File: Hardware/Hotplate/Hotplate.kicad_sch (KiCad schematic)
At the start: 23 parts, among them J4 Conn_01x01_Pin, J5 Conn_01x01_Pin, Q2 Q_NMOS_GDS, SW1 SW_Push, SW2 SW_Push, SW3 SW_Push, SW4 SW_Push, U1 STM32F301K6Tx

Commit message: V2
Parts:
- removed J4, J5: Conn_01x01_Pin, Connector_Wire:SolderWire-1.5sqmm_1x01_D1.7mm_OD3mm, symbol Connector:Conn_01x01_Pin
- removed Q2: Q_NMOS_GDS, Package_TO_SOT_SMD:TO-252-2, symbol Device:Q_NMOS_GDS
- removed R2: 1k, Resistor_SMD:R_0805_2012Metric, symbol Device:R
- removed R3: 100k, Resistor_SMD:R_0805_2012Metric, symbol Device:R
- added C11: 1uF, Capacitor_SMD:C_0603_1608Metric, symbol Device:C
- added D7: D_Schottky, Diode_THT:D_DO-15_P10.16mm_Horizontal, symbol Device:D_Schottky
- added IC2: MCP1402T-E_OT, SOT95P270X145-5N, symbol SamacSys_Parts:MCP1402T-E_OT
- added Q1: BSC146N10LS5ATMA1, SamacSys_Parts:BSC146N10LS5ATMA1, symbol SamacSys_Parts:BSC146N10LS5ATMA1
- added R11: 270, Resistor_SMD:R_0603_1608Metric_Pad0.98x0.95mm_HandSolder, symbol Device:R_Small
- C1, C2: value C -> 100nF
- C3: value C -> 10nF
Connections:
- net GND: now also C11.1, IC2.1 (GND_1), IC2.4 (GND_2), Q1.1 (S_1), Q1.2 (S_2), Q1.3 (S_3)
- net VCC: now also D7.1 (K)
- net Drain: now reaches NT1.1
- net Drain: now also D7.2 (A), Q1.5 (D_1), Q1.6 (D_2), Q1.7 (D_3), Q1.8 (D_4), Q1.9 (D_5)
- net PA2 | TIM2_CH3: now reaches U1.8 (PA2)
- net PA2 | TIM2_CH3: now also IC2.3 (IN)
- new net: IC2.5 (OUT), R11.1
- new net +5V: C11.2, IC2.2 (VDD)
- new net Gate: Q1.4 (G), R11.2
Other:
- note added: "MCU"
- note added: "MOSFET Driver"
- note added: "Mounting Holes"
- moved on the sheet: C1, C2, C3, C6, D5, D6, H1, H2, H3, H4, NT1, R17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

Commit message: made it pretty (#8)
Co-authored-by: nexophoenixe <jan.gradwohl2005@mail.com>
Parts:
- renumbered C2 to C101, C1 to C102, C6 to C103, C3 to C104, C11 to C105, D5 to D101, D6 to D102, D7 to D103, H1 to H101, H2 to H102, H3 to H103, H4 to H104, IC2 to IC101, NT1 to NT101, Q1 to Q101, R17 to R101, R8 to R102, R11 to R103, SW4 to SW101, SW3 to SW102, SW2 to SW103, SW1 to SW104, U1 to U101
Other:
- note added: "Buttons"
- note added: "Debugging LEDs"
- note added: "Power Side"
- moved on the sheet: C101, C102, C103, C104, C105, IC101, R103, SW101, SW102, SW103, SW104, U101

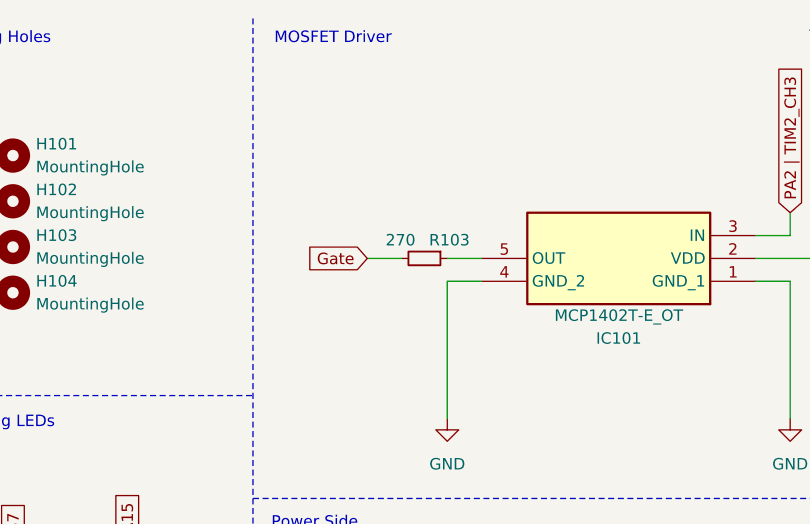
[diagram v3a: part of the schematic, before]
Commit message: Debug (#15)
* fixed:PID

* fixed:PID

* fixed:dyingFETs
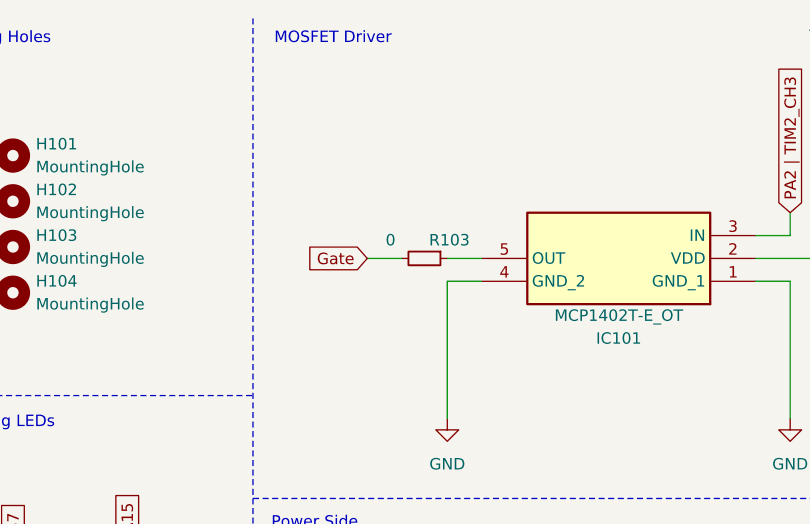
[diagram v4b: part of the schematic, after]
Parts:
- R103: value 270 -> 0
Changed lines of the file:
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@@
 			)
 		)
-		(property "Value" "270"
+		(property "Value" "0"
 			(at 146.812 37.338 90)
 			(effects
